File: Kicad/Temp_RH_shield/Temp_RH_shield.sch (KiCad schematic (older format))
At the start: 12 parts, among them J1 Temp_RH_Module, J10 CONN_02X01, J2 micro_SD, J3 RTC, J4 Screw_Terminal_1x02, J5 CONN_01X01, J6 CONN_01X01, J7 CONN_01X01, J8 CONN_02X01, J9 CONN_02X01

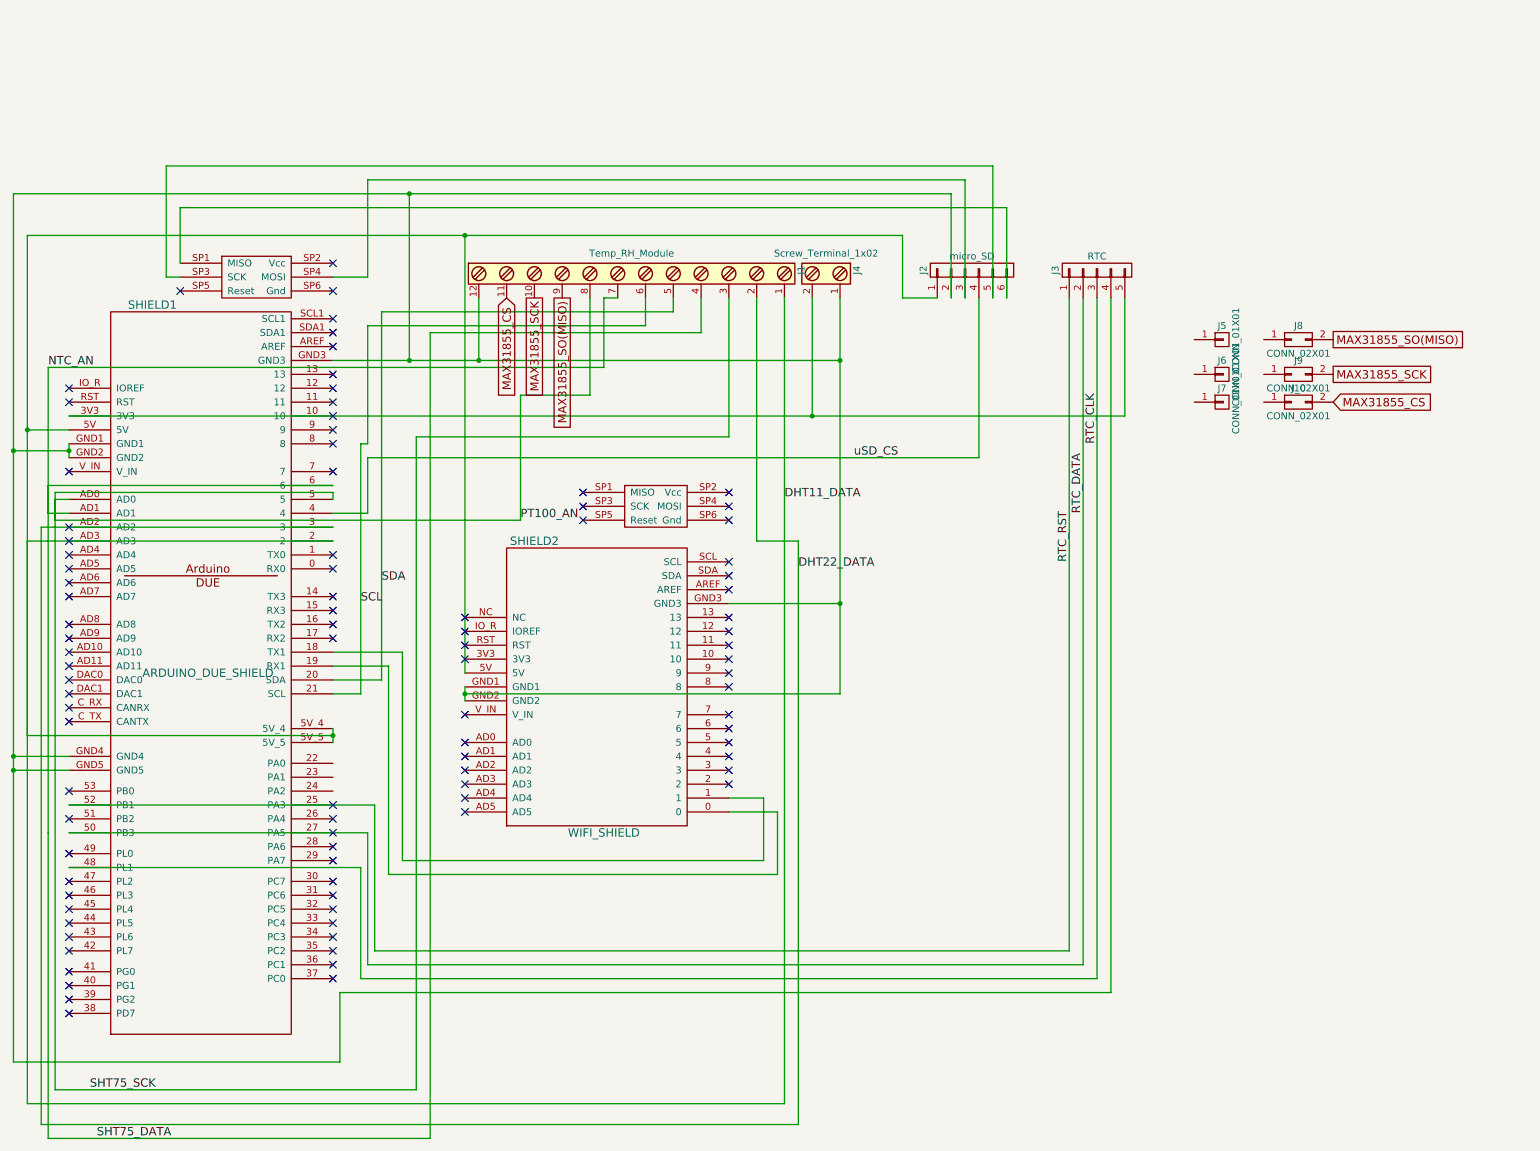
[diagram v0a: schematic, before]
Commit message: Changes made on the file structure (not yet finished). Added Arduino project for Gas, Current, Motion, Reed and Distance sensors (GCMRD). Modifyed Temp_HR  shield to add the MLX sensor.
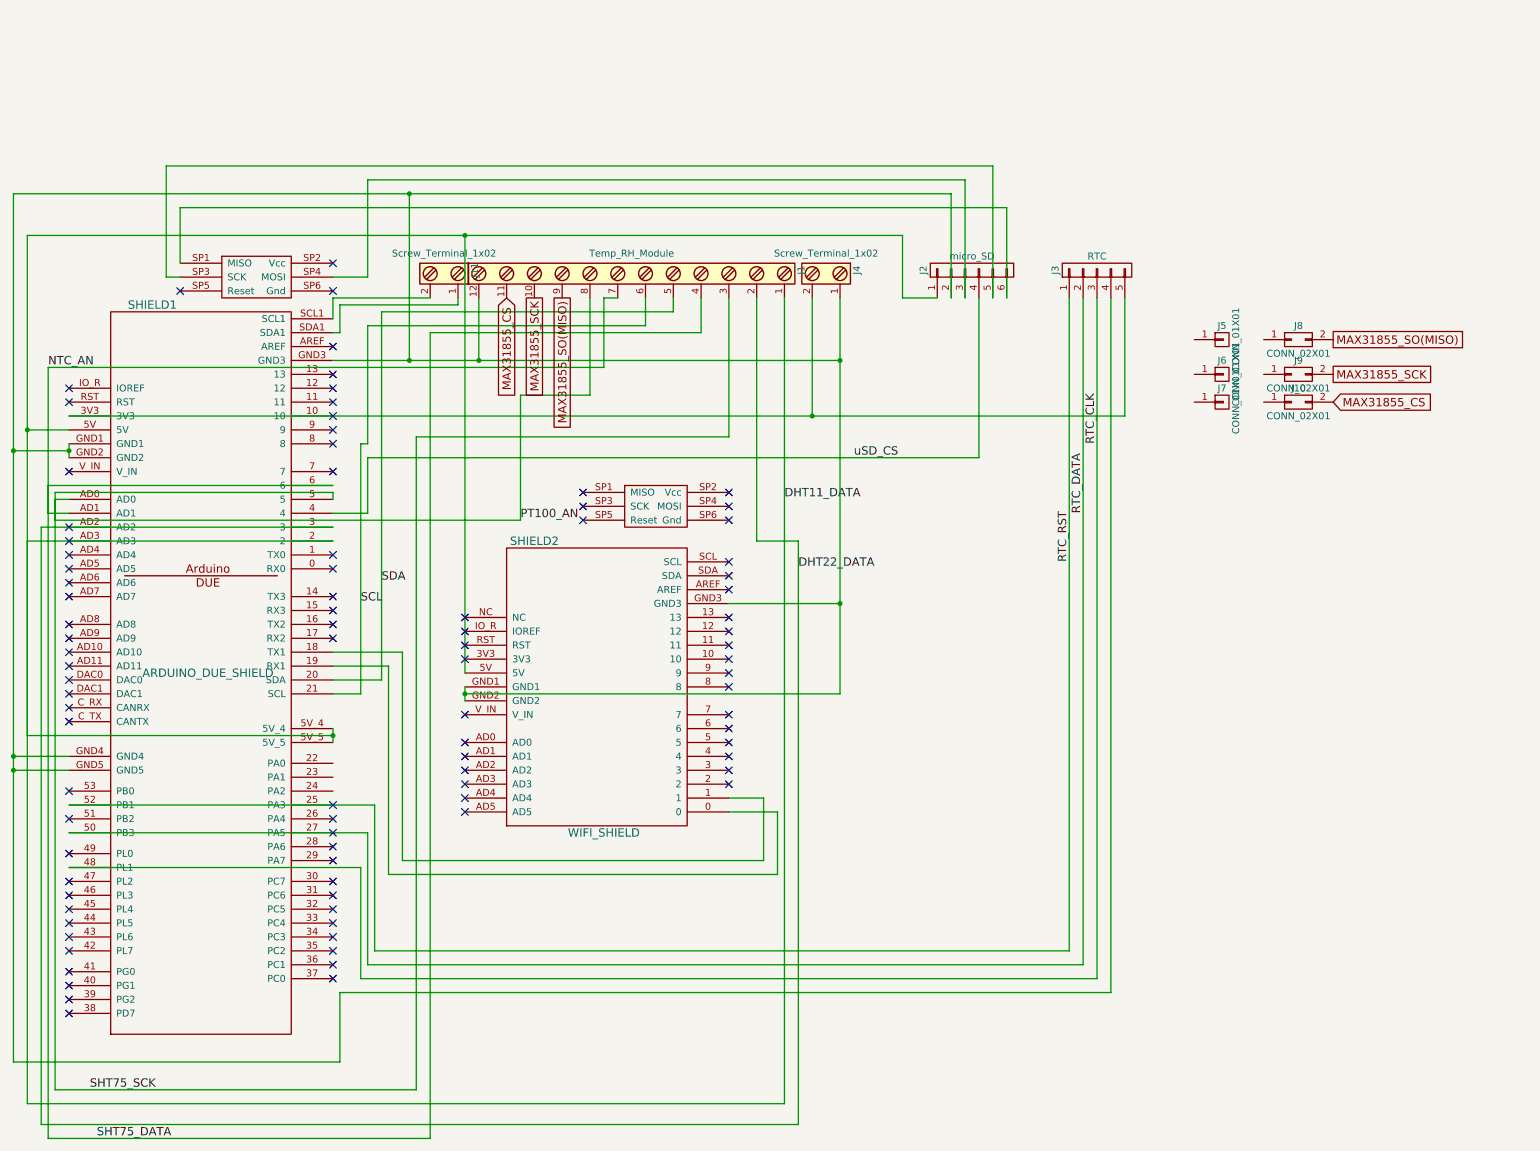
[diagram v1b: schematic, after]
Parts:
- added J11: Screw_Terminal_1x02, Connectors_Terminal_Blocks:TerminalBlock_Pheonix_PT-3.5mm_2pol, symbol Screw_Terminal_1x02
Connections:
- net at SHIELD1.SCL1: now also J11.2
- net at SHIELD1.SDA1: now also J11.1
- no-connect marks 94 -> 92
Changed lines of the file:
@@
 LIBS:valves
 LIBS:freetronics_schematic
+LIBS:Temp_RH_shield-cache
 EELAYER 25 0
 EELAYER END
@@
 NoConn ~ 6250 3000
 NoConn ~ 6250 3100
-NoConn ~ 3400 1650
-NoConn ~ 3400 1750
 NoConn ~ 3400 1850
 NoConn ~ 3400 2050
@@
 	4350 4200 4350 1050
 Wire Wire Line
-	1200 1050 4350 1050
-Wire Wire Line
-	4350 1050 7500 1050
-Wire Wire Line
-	1200 1050 1200 2450
-Wire Wire Line
-	1200 2450 1200 4650
+	1200 1050 7500 1050
+Wire Wire Line
+	1200 1050 1200 4650
 Wire Wire Line
 	1200 2450 1500 2450
@@
 	1100 4800 1500 4800
 Wire Wire Line
-	1100 750  1100 2600
-Wire Wire Line
-	1100 2600 1100 4800
-Wire Wire Line
-	1100 4800 1100 4900
-Wire Wire Line
-	1100 4900 1100 7000
-Wire Wire Line
-	1100 750  3950 750
-Wire Wire Line
-	3950 750  7850 750
+	1100 750  1100 7000
+Wire Wire Line
+	1100 750  7850 750
 Wire Wire Line
 	7850 750  7850 1500
@@
 	9100 2350 9100 1500
 Wire Wire Line
-	1500 2350 6850 2350
-Wire Wire Line
-	6850 2350 9100 2350
+	1500 2350 9100 2350
 Wire Wire Line
 	9000 1500 9000 6500
@@
 	1100 4900 1500 4900
 Wire Wire Line
-	7050 1500 7050 1950
-Wire Wire Line
-	7050 1950 7050 3700
-Wire Wire Line
-	7050 3700 7050 4350
-Wire Wire Line
-	3400 1950 3950 1950
-Wire Wire Line
-	3950 1950 4450 1950
-Wire Wire Line
-	4450 1950 7050 1950
+	7050 1500 7050 4350
+Wire Wire Line
+	3400 1950 7050 1950
 Wire Wire Line
 	6850 1500 6850 2350
@@
 	4100 7550 1350 7550
 Wire Wire Line
-	1350 7550 1350 5350
-Wire Wire Line
-	1350 5350 1350 2850
+	1350 7550 1350 2850
 Wire Wire Line
 	6250 1500 6250 2500
@@
 	7050 4350 4350 4350
 Wire Wire Line
-	4350 4300 4350 4350
-Wire Wire Line
-	4350 4350 4350 4400
+	4350 4300 4350 4400
 Connection ~ 7050 1950
 Connection ~ 4350 4350
@@
 Connection ~ 1100 4900
 Wire Wire Line
-	1500 2550 1500 2600
-Wire Wire Line
-	1500 2600 1500 2650
+	1500 2550 1500 2650
 Wire Wire Line
 	1100 2600 1500 2600
@@
 RTC_RST
 Wire Wire Line
-	3400 4600 3400 4650
-Wire Wire Line
-	3400 4650 3400 4700
+	3400 4600 3400 4700
 Wire Wire Line
 	1200 4650 3400 4650
@@
 	1    0    0    -1
 $EndComp
+$Comp
+L Screw_Terminal_1x02 J11
+U 1 1 5976AABE
+P 4200 1300
+F 0 "J11" H 4200 1550 50  0000 C TNN
+F 1 "Screw_Terminal_1x02" V 4050 1300 50  0000 C TNN
+F 2 "Connectors_Terminal_Blocks:TerminalBlock_Pheonix_PT-3.5mm_2pol" H 4200 1075 50  0001 C CNN
+F 3 "" H 4175 1300 50  0001 C CNN
+	1    4200 1300
+	0    1    1    0
+$EndComp
+Wire Wire Line
+	4100 1500 3400 1500
+Wire Wire Line
+	3400 1500 3400 1650
+Wire Wire Line
+	4300 1500 4300 1550
+Wire Wire Line
+	4300 1550 3450 1550
+Wire Wire Line
+	3450 1550 3450 1750
+Wire Wire Line
+	3450 1750 3400 1750
 $EndSCHEMATC

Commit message: Added PT100 conditioning circuit to Tem_HR shield. Ready for testing!
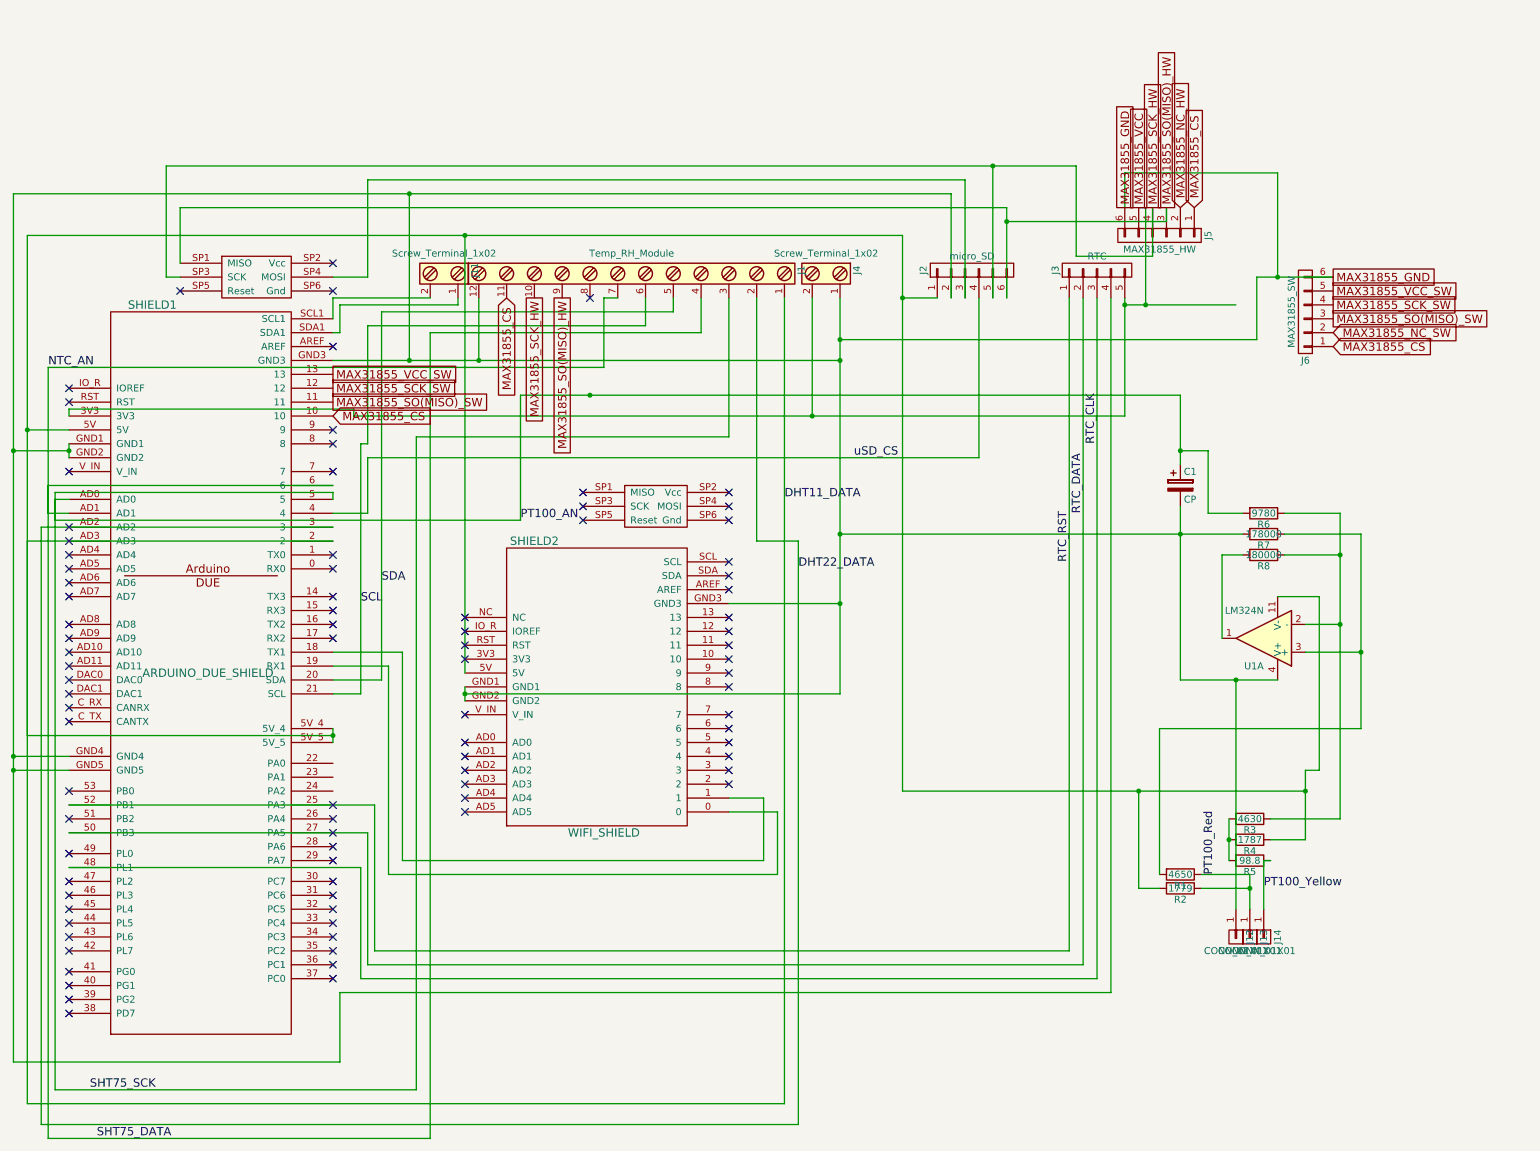
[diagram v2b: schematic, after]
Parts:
- removed J10, J8, J9: CONN_02X01, Pin_Headers:Pin_Header_Straight_2x01_Pitch2.54mm, symbol CONN_02X01
- removed J5, J6, J7: CONN_01X01, Pin_Headers:Pin_Header_Straight_1x01_Pitch2.54mm, symbol CONN_01X01
- added C1: CP, Capacitors_THT:CP_Radial_D6.3mm_P2.50mm, symbol CP
- added J12, J13, J14: CONN_01X01, Pin_Headers:Pin_Header_Straight_1x01_Pitch2.54mm, symbol CONN_01X01
- added J5: MAX31855_HW, Pin_Headers:Pin_Header_Straight_1x06_Pitch2.54mm, symbol CONN_01X06
- added J6: MAX31855_SW, Pin_Headers:Pin_Header_Straight_1x06_Pitch2.54mm, symbol CONN_01X06
- added R1: 4650, Resistors_THT:R_Axial_DIN0309_L9.0mm_D3.2mm_P12.70mm_Horizontal, symbol R
- added R2: 1779, Resistors_THT:R_Axial_DIN0309_L9.0mm_D3.2mm_P12.70mm_Horizontal, symbol R
- added R3: 4630, Resistors_THT:R_Axial_DIN0309_L9.0mm_D3.2mm_P12.70mm_Horizontal, symbol R
- added R4: 1787, Resistors_THT:R_Axial_DIN0309_L9.0mm_D3.2mm_P12.70mm_Horizontal, symbol R
- added R5: 98.8, Resistors_THT:R_Axial_DIN0309_L9.0mm_D3.2mm_P12.70mm_Horizontal, symbol R
- added R6: 9780, Resistors_THT:R_Axial_DIN0309_L9.0mm_D3.2mm_P12.70mm_Horizontal, symbol R
- added R7: 178000, Resistors_THT:R_Axial_DIN0309_L9.0mm_D3.2mm_P12.70mm_Horizontal, symbol R
- added R8: 180000, Resistors_THT:R_Axial_DIN0309_L9.0mm_D3.2mm_P12.70mm_Horizontal, symbol R
- added U1: LM324N, Housings_DIP:DIP-14_W7.62mm_Socket, symbol LM324N
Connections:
- net MAX31855_SCK is gone; now on net MAX31855_SCK_HW: J1.10
- net MAX31855_SO(MISO) is gone; now on net MAX31855_SO(MISO)_HW: J1.9
- net DHT11_DATA: now also R2.2, R4.1, U1.11 (V-)
- net MAX31855_CS: now also SHIELD1.10, J5.1 (P1), J6.1 (P1)
- net PT100_AN: now also C1.1, R6.2; no longer J1.8
- net MAX31855_SO(MISO)_SW: now reaches SHIELD1.11
- net MAX31855_SO(MISO)_SW: now also J6.3 (P3)
- net MAX31855_SCK_SW: now reaches SHIELD1.12
- net MAX31855_SCK_SW: now also J6.4 (P4)
- net MAX31855_VCC_SW: now reaches SHIELD1.13
- net MAX31855_VCC_SW: now also J6.5 (P5)
- net MAX31855_VCC: now reaches J3.5 (P5), J4.2, SHIELD1.3V3
- net MAX31855_VCC: now also J5.5 (P5)
- net MAX31855_GND: now reaches J1.12, J2.2 (P2), J3.4 (P4), J4.1, SHIELD1.GND1, SHIELD1.GND2, SHIELD1.GND3, SHIELD1.GND4, SHIELD1.GND5, SHIELD2.GND1, SHIELD2.GND2, SHIELD2.GND3
- net MAX31855_GND: now also C1.2, J12.1 (P1), J5.6 (P6), J6.6 (P6), R7.2, U1.4 (V+)
- net MAX31855_SO(MISO)_HW: now reaches J2.6 (P6), SHIELD1.SP1 (MISO)
- net MAX31855_SO(MISO)_HW: now also J5.3 (P3)
- net MAX31855_SCK_HW: now reaches J2.5 (P5), SHIELD1.SP3 (SCK)
- net MAX31855_SCK_HW: now also J5.4 (P4)
- new net: R8.2, U1.1
- new net: R3.1, R6.1, R8.1, U1.2 (-)
- new net: R1.2, R7.1, U1.3 (+)
- new net: R3.2, R4.2, R5.2
- new net MAX31855_NC_HW: J5.2 (P2)
- new net MAX31855_NC_SW: J6.2 (P2)
- new net PT100_Red: J13.1 (P1), R1.1, R2.1
- new net PT100_Yellow: J14.1 (P1), R5.1
- no-connect marks 92 -> 89
